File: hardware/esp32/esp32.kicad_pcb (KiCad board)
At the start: 4 copper layers, 32.8 x 36.3 mm, 69 parts, among them J1 PlugIn_Terminal_01x02, J2 ESP_left, J3 ESP_right, J4 PlugIn_Terminal_01x02, J5 Plugged into C8387, Q1 MMBT5401, Q2 MMBT2222A, U2 LMV321, U3 LMV321, U6 LM393

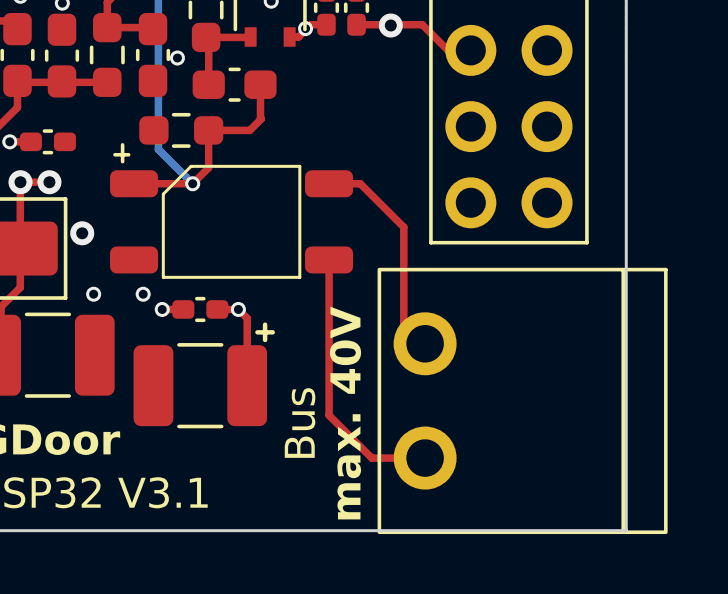
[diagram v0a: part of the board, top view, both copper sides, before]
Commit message: Release HW3.1-1
Changed bus connector due to JLCPCB availability
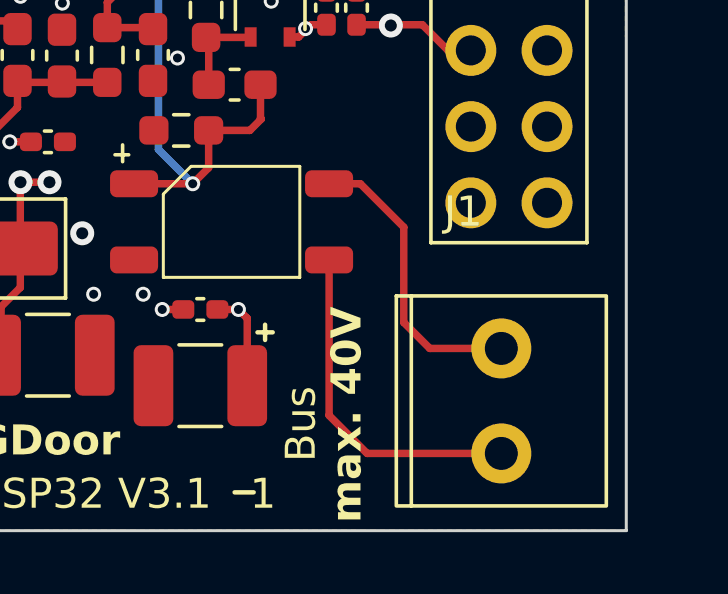
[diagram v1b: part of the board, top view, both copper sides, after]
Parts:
- removed J5: Plugged into C8387, Library:nofoorprint
- J1: value PlugIn_Terminal_01x02 -> PlugIn_Terminal_Screw; footprint Library:steckklemme2x1_1 -> Library:anschlussklemme2x1_3_5
- moved J1 2.54 mm to (140.7, 109.7)
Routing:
- net Net-(J1-Pin_1): track 7.27 -> 9.88 mm
- net Net-(J1-Pin_2): track 8.97 -> 11.4 mm
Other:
- board text added: "1"
- board text removed: "Connector C8466 (J5) plugged into C8387 (J1)"
- board text removed: "J5"
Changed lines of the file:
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@@
     )
   )
-  (footprint "Library:nofoorprint" (layer "F.Cu")
-    (at 153.543 109.3978)
-    (property "MPN" "C8466")
-    (property "Sheetfile" "esp32.kicad_sch")
-    (property "Sheetname" "")
-    (attr smd)
-    (fp_text reference "J5" (at 0 -0.5 unlocked) (layer "F.SilkS") hide
-        (effects (font (size 1 1) (thickness 0.1)))
-    )
-    (fp_text value "Plugged into C8387" (at 0 1 unlocked) (layer "F.Fab")
-        (effects (font (size 1 1) (thickness 0.15)))
-    )
-    (fp_text user "${REFERENCE}" (at 0 2.5 unlocked) (layer "F.Fab")
-        (effects (font (size 1 1) (thickness 0.15)))
-    )
-    (fp_rect (start -4.826 -5.08) (end 5.334 5.842)
-      (stroke (width 0.05) (type default)) (fill none) (layer "F.CrtYd"))
-  )
   (footprint "Library:C_0603_1608Metric_Pad1.08x0.95mm_HandSolder" (layer "F.Cu")
     (at 131.826 99.187)
@@
     )
   )
-  (footprint "Library:steckklemme2x1_1" (layer "F.Cu")
-    (at 138.176 109.728)
+  (footprint "Library:anschlussklemme2x1_3_5" (layer "F.Cu")
+    (at 140.716 109.728)
     (property "JLCPCB Rotation Offset" "90")
     (property "JlcRotOffset" "-180")
-    (property "MPN" "C8387")
+    (property "MPN" "C695629")
     (property "Sheetfile" "esp32.kicad_sch")
     (property "Sheetname" "")
@@
     (property "ki_keywords" "screw terminal")
     (attr through_hole)
-    (fp_text reference "J1" (at -1.27 -6.31 unlocked) (layer "F.SilkS") hide
+    (fp_text reference "J1" (at -1.27 -6.31 unlocked) (layer "F.SilkS")
         (effects (font (size 1 1) (thickness 0.15)))
     )
-    (fp_text value "PlugIn_Terminal_01x02" (at 0 -1.5 unlocked) (layer "F.Fab")
+    (fp_text value "PlugIn_Terminal_Screw" (at 0 -1.5 unlocked) (layer "F.Fab")
         (effects (font (size 1 1) (thickness 0.15)))
     )
@@
         (effects (font (size 1 1) (thickness 0.15)))
     )
-    (fp_line (start 6.604 -4.318) (end 6.604 4.318)
+    (fp_line (start -3 -3.5) (end -3 3.5)
       (stroke (width 0.12) (type solid)) (layer "F.SilkS"))
-    (fp_rect (start 8.024 -4.377) (end -1.524 4.377)
+    (fp_rect (start -3.5 -3.5) (end 3.5 3.5)
       (stroke (width 0.12) (type solid)) (fill none) (layer "F.SilkS"))
-    (pad "1" thru_hole circle (at 0 -1.905) (size 2.1 2.1) (drill 1.25) (layers "*.Cu" "*.Mask")
+    (pad "1" thru_hole circle (at 0 -1.75) (size 2 2) (drill 1.1) (layers "*.Cu" "*.Mask")
       (net 12 "Net-(J1-Pin_1)") (pinfunction "Pin_1") (pintype "passive"))
-    (pad "2" thru_hole circle (at 0 1.905) (size 2.1 2.1) (drill 1.25) (layers "*.Cu" "*.Mask")
+    (pad "2" thru_hole circle (at 0 1.75) (size 2 2) (drill 1.1) (layers "*.Cu" "*.Mask")
       (net 13 "Net-(J1-Pin_2)") (pinfunction "Pin_2") (pintype "passive"))
-    (model "${KIPRJMOD}/3dmodels/screwterminal.stp"
-      (offset (xyz 8 4.22 7))
+    (model "${KIPRJMOD}/3dmodels/screwterminal_3_5mm_2.STEP"
+      (offset (xyz 3.6 -3.5 0))
       (scale (xyz 1 1 1))
-      (rotate (xyz 180 0 90))
+      (rotate (xyz -90 0 -90))
     )
   )
@@
   (gr_circle (center 142.24 87.884) (end 143.129 88.265)
     (stroke (width 0.15) (type default)) (fill none) (layer "B.SilkS"))
-  (gr_rect (start 136.525 105.537) (end 141.478 113.411)
+  (gr_rect (start 138.7475 105.537) (end 143.7005 113.411)
     (stroke (width 0.15) (type default)) (fill none) (layer "B.SilkS"))
   (gr_line (start 125.781295 107.297593) (end 125.789967 107.292438)
@@
   (gr_line (start 122.428 107.315) (end 122.936 107.315)
     (stroke (width 0.15) (type default)) (layer "F.SilkS"))
+  (gr_line (start 131.826 112.776) (end 132.461 112.776)
+    (stroke (width 0.15) (type default)) (layer "F.SilkS"))
   (gr_line (start 122.682 107.061) (end 122.682 107.569)
     (stroke (width 0.15) (type default)) (layer "F.SilkS"))
@@
   (gr_line (start 120.65 111.76) (end 122.174 111.76)
     (stroke (width 0.3) (type default)) (layer "F.SilkS"))
-  (gr_line (start 148.59 108.966) (end 146.939 109.728)
-    (stroke (width 0.15) (type default)) (layer "Cmts.User"))
-  (gr_line (start 155.575 109.728) (end 146.939 109.728)
-    (stroke (width 0.15) (type default)) (layer "Cmts.User"))
-  (gr_line (start 146.939 109.728) (end 148.59 108.966)
-    (stroke (width 0.15) (type default)) (layer "Cmts.User"))
-  (gr_line (start 148.59 110.49) (end 146.939 109.728)
-    (stroke (width 0.15) (type default)) (layer "Cmts.User"))
   (gr_rect (start 112.052 77.743) (end 144.8816 114.0524)
     (stroke (width 0.1) (type default)) (fill none) (layer "Edge.Cuts"))
@@
     (effects (font (size 1 1) (thickness 0.15)) (justify left bottom mirror))
   )
-  (gr_text "A" (at 140.208 107.9754) (layer "B.SilkS")
+  (gr_text "A" (at 139.319 107.061) (layer "B.SilkS")
     (effects (font (size 1 1) (thickness 0.15)) (justify bottom mirror))
   )
@@
     (effects (font (size 1 1) (thickness 0.15)) (justify left top mirror))
   )
-  (gr_text "Bus" (at 142.0368 109.1692 270) (layer "B.SilkS")
+  (gr_text "Bus" (at 142.24 109.728 270) (layer "B.SilkS")
     (effects (font (size 1 1) (thickness 0.2) bold) (justify bottom mirror))
   )
@@
     (effects (font (size 1 1) (thickness 0.2) bold) (justify left bottom mirror))
   )
-  (gr_text "B" (at 140.1826 111.8616) (layer "B.SilkS")
+  (gr_text "B" (at 139.319 113.157) (layer "B.SilkS")
     (effects (font (size 1 1) (thickness 0.15)) (justify bottom mirror))
   )
@@
     (effects (font (size 1 1) (thickness 0.25) bold) (justify left bottom))
   )
+  (gr_text "1" (at 132.334 113.411) (layer "F.SilkS")
+    (effects (font (size 1 1) (thickness 0.15)) (justify left bottom))
+  )
   (gr_text "ESP32 V3.1" (at 123.19 113.411) (layer "F.SilkS")
     (effects (font (size 1 1) (thickness 0.15)) (justify left bottom))
@@
     (effects (font (size 1 1) (thickness 0.15)) (justify left bottom))
   )
-  (gr_text "J5" (at 152.654 112.522) (layer "Cmts.User")
-    (effects (font (size 1 1) (thickness 0.15)) (justify left bottom))
-  )
-  (gr_text "Connector C8466 (J5)\nplugged into C8387 (J1)" (at 141.478 117.729) (layer "Cmts.User")
-    (effects (font (size 1 1) (thickness 0.15)) (justify left bottom))
-  )
   (dimension (type aligned) (layer "User.1")
     (pts (xy 144.8816 77.7748) (xy 144.907 72.6186))
@@
   (segment (start 129.0563 97.2839) (end 129.1063 97.3339) (width 0.25) (layer "F.Cu") (net 11))
   (segment (start 128.0884 94.1832) (end 128.0884 95.6564) (width 0.25) (layer "F.Cu") (net 11))
-  (segment (start 136.017 102.489) (end 134.9744 102.489) (width 0.25) (layer "F.Cu") (net 12))
-  (segment (start 138.176 107.823) (end 137.4648 107.1118) (width 0.25) (layer "F.Cu") (net 12))
-  (segment (start 137.4648 107.1118) (end 137.4648 103.9368) (width 0.25) (layer "F.Cu") (net 12))
-  (segment (start 137.4648 103.9368) (end 136.017 102.489) (width 0.25) (layer "F.Cu") (net 12))
+  (segment (start 137.4648 103.9368) (end 137.4648 107.1118) (width 0.25) (layer "F.Cu") (net 12))
+  (segment (start 136.017 102.489) (end 137.4648 103.9368) (width 0.25) (layer "F.Cu") (net 12))
+  (segment (start 138.331 107.978) (end 140.716 107.978) (width 0.25) (layer "F.Cu") (net 12))
+  (segment (start 134.9744 102.489) (end 136.017 102.489) (width 0.25) (layer "F.Cu") (net 12))
+  (segment (start 137.4648 107.1118) (end 138.331 107.978) (width 0.25) (layer "F.Cu") (net 12))
   (segment (start 134.9744 105.029) (end 134.9744 110.2094) (width 0.25) (layer "F.Cu") (net 13))
-  (segment (start 136.398 111.633) (end 138.176 111.633) (width 0.25) (layer "F.Cu") (net 13))
-  (segment (start 134.9744 110.2094) (end 136.398 111.633) (width 0.25) (layer "F.Cu") (net 13))
+  (segment (start 136.243 111.478) (end 140.716 111.478) (width 0.25) (layer "F.Cu") (net 13))
+  (segment (start 134.9744 110.2094) (end 136.243 111.478) (width 0.25) (layer "F.Cu") (net 13))
   (segment (start 130.3141 83.2872) (end 130.9226 82.6787) (width 0.25) (layer "F.Cu") (net 14))
   (segment (start 130.9226 82.6787) (end 130.9226 82.2173) (width 0.25) (layer "F.Cu") (net 14))

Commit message: work on V4.0
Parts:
- added C21: 100u TBD check voltage, Library:C_1210_3225Metric_Pad1.33x2.70mm_HandSolder, F.Cu at (109.2, 97.4)
- added C22: 100n, Library:C_0603_1608Metric_Pad1.08x0.95mm_HandSolder, F.Cu at (100.6, 87.8)
- added C23: 10u, Library:C_0603_1608Metric_Pad1.08x0.95mm_HandSolder, F.Cu at (105.5, 87.8)
- added C24: 100n, Library:C_0603_1608Metric_Pad1.08x0.95mm_HandSolder, F.Cu at (104.0, 87.8)
- added C25: 10u, Library:C_0603_1608Metric_Pad1.08x0.95mm_HandSolder, F.Cu at (108.7, 93.2)
- added C26: 100n, Library:C_0603_1608Metric_Pad1.08x0.95mm_HandSolder, F.Cu at (107.2, 93.2)
- added C27: 10u, Library:C_0603_1608Metric_Pad1.08x0.95mm_HandSolder, F.Cu at (105.5, 93.2)
- added C28: 10u, Library:C_0603_1608Metric_Pad1.08x0.95mm_HandSolder, F.Cu at (107.1, 80.9)
- added C29: 10u, Library:C_0603_1608Metric_Pad1.08x0.95mm_HandSolder, F.Cu at (107.1, 79.4)
- added C30: 10u, Library:C_0603_1608Metric_Pad1.08x0.95mm_HandSolder, F.Cu at (107.1, 84.7)
- added C31: 10u, Library:C_0603_1608Metric_Pad1.08x0.95mm_HandSolder, F.Cu at (107.1, 83.2)
- added C32: 100n, Library:C_0603_1608Metric_Pad1.08x0.95mm_HandSolder, F.Cu at (102.2, 102.5)
- added C33: 100n, Library:C_0603_1608Metric_Pad1.08x0.95mm_HandSolder, F.Cu at (107.3, 108.7)
- added C34: 100n, Library:C_0603_1608Metric_Pad1.08x0.95mm_HandSolder, F.Cu at (104.0, 93.2)
- added C35: 10u, Library:C_0603_1608Metric_Pad1.08x0.95mm_HandSolder, F.Cu at (102.1, 87.8)
- added C36: 100n, Library:C_0402_1005Metric_Pad0.74x0.62mm_HandSolder, F.Cu at (99.9, 95.5)
- added C37: 10u, Library:C_0603_1608Metric_Pad1.08x0.95mm_HandSolder, F.Cu at (92.5, 102.6)
- added C38: 100n, Library:C_0402_1005Metric_Pad0.74x0.62mm_HandSolder, F.Cu at (94.6, 92.5)
- added C39: 10u, Library:C_0603_1608Metric_Pad1.08x0.95mm_HandSolder, F.Cu at (86.4, 102.6)
- added C40: 100n, Library:C_0402_1005Metric_Pad0.74x0.62mm_HandSolder, F.Cu at (94.6, 94.1)
- added C41: 10u, Library:C_0603_1608Metric_Pad1.08x0.95mm_HandSolder, F.Cu at (89.4, 102.6)
- added C42: 100n, Library:C_0402_1005Metric_Pad0.74x0.62mm_HandSolder, F.Cu at (102.0, 93.2)
- added C43: 10u, Library:C_0603_1608Metric_Pad1.08x0.95mm_HandSolder, F.Cu at (95.5, 102.6)
- added C44: 22p, Library:C_0603_1608Metric_Pad1.08x0.95mm_HandSolder, F.Cu at (89.7, 91.9)
- added C45: 22p, Library:C_0603_1608Metric_Pad1.08x0.95mm_HandSolder, F.Cu at (93.6, 88.5)
- added C46: 100n, Library:C_0402_1005Metric_Pad0.74x0.62mm_HandSolder, F.Cu at (86.6, 107.0)
- added C47: 10u, Library:C_0603_1608Metric_Pad1.08x0.95mm_HandSolder, F.Cu at (87.9, 107.2)
- added C48: 22p, Library:C_0603_1608Metric_Pad1.08x0.95mm_HandSolder, F.Cu at (92.6, 95.4)
- added C49: 22p, Library:C_0603_1608Metric_Pad1.08x0.95mm_HandSolder, F.Cu at (96.6, 98.0)
- added C50: 22p, Library:C_0603_1608Metric_Pad1.08x0.95mm_HandSolder, F.Cu at (92.7, 91.9)
- added C51: 100n, Library:C_0402_1005Metric_Pad0.74x0.62mm_HandSolder, F.Cu at (89.7, 107.0)
- added C52: 10u, Library:C_0603_1608Metric_Pad1.08x0.95mm_HandSolder, F.Cu at (90.9, 107.2)
- added C53: 100n, Library:C_0402_1005Metric_Pad0.74x0.62mm_HandSolder, F.Cu at (92.7, 107.0)
- added C54: 10u, Library:C_0603_1608Metric_Pad1.08x0.95mm_HandSolder, F.Cu at (94.0, 107.2)
- added C55: 100n, Library:C_0402_1005Metric_Pad0.74x0.62mm_HandSolder, F.Cu at (95.8, 107.0)
- added C56: 10u, Library:C_0603_1608Metric_Pad1.08x0.95mm_HandSolder, F.Cu at (97.0, 107.2)
- added C57: 100u, Library:C_1210_3225Metric_Pad1.33x2.70mm_HandSolder, F.Cu at (107.0, 111.1)
- added C59: 100u, Library:C_1210_3225Metric_Pad1.33x2.70mm_HandSolder, F.Cu at (99.8, 107.4)
- added C61: 22p, Library:C_0603_1608Metric_Pad1.08x0.95mm_HandSolder, F.Cu at (103.5, 105.8)
- added C62: 100n, Library:C_0402_1005Metric_Pad0.74x0.62mm_HandSolder, F.Cu at (102.4, 84.7)
- added C63: 100n, Library:C_0402_1005Metric_Pad0.74x0.62mm_HandSolder, F.Cu at (102.4, 80.6)
- added R35: 82k, Library:R_0603_1608Metric_Pad0.98x0.95mm_HandSolder, F.Cu at (110.6, 88.0)
- added R37: 1k, Library:R_0603_1608Metric_Pad0.98x0.95mm_HandSolder, F.Cu at (91.8, 84.4)
- added R38: 1k, Library:R_0603_1608Metric_Pad0.98x0.95mm_HandSolder, F.Cu at (88.8, 84.4)
- added R39: 1k, Library:R_0603_1608Metric_Pad0.98x0.95mm_HandSolder, F.Cu at (97.9, 84.4)
- added R40: 1k, Library:R_0603_1608Metric_Pad0.98x0.95mm_HandSolder, F.Cu at (94.9, 84.4)
- added R41: 33, Library:R_0603_1608Metric_Pad0.98x0.95mm_HandSolder, F.Cu at (97.0, 102.6)
- added R42: 33, Library:R_0603_1608Metric_Pad0.98x0.95mm_HandSolder, F.Cu at (90.9, 102.6)
- added R43: 33, Library:R_0603_1608Metric_Pad0.98x0.95mm_HandSolder, F.Cu at (87.9, 102.6)
- added R44: 33, Library:R_0603_1608Metric_Pad0.98x0.95mm_HandSolder, F.Cu at (94.0, 102.6)
- added R45: 10k, Library:R_0402_1005Metric_Pad0.72x0.64mm_HandSolder, F.Cu at (94.9, 88.9)
- added R46: 2k4, Library:R_0603_1608Metric_Pad0.98x0.95mm_HandSolder, F.Cu at (90.6, 88.5)
- added R47: 2k4, Library:R_0603_1608Metric_Pad0.98x0.95mm_HandSolder, F.Cu at (88.1, 95.4)
- added R48: 100, Library:R_0603_1608Metric_Pad0.98x0.95mm_HandSolder, F.Cu at (88.1, 91.9)
- added R49: 100, Library:R_0603_1608Metric_Pad0.98x0.95mm_HandSolder, F.Cu at (92.1, 88.5)
- added R50: 33, Library:R_0603_1608Metric_Pad0.98x0.95mm_HandSolder, F.Cu at (91.2, 91.9)
- added R51: 33, Library:R_0603_1608Metric_Pad0.98x0.95mm_HandSolder, F.Cu at (95.1, 98.0)
- added R52: 33, Library:R_0603_1608Metric_Pad0.98x0.95mm_HandSolder, F.Cu at (92.6, 96.9)
- added R53: 33, Library:R_0603_1608Metric_Pad0.98x0.95mm_HandSolder, F.Cu at (92.6, 99.4)
- added R54: 33, Library:R_0603_1608Metric_Pad0.98x0.95mm_HandSolder, F.Cu at (98.2, 98.0)
- added R55: 0, Library:R_0603_1608Metric_Pad0.98x0.95mm_HandSolder, F.Cu at (99.7, 101.6)
- added R56: 0, Library:R_0603_1608Metric_Pad0.98x0.95mm_HandSolder, F.Cu at (120.7, 80.0)
- added R57: 0, Library:R_0603_1608Metric_Pad0.98x0.95mm_HandSolder, F.Cu at (110.5, 111.1)
- added R58: 0, Library:R_0603_1608Metric_Pad0.98x0.95mm_HandSolder, F.Cu at (99.7, 103.4)
- added R59: 0, Library:R_0603_1608Metric_Pad0.98x0.95mm_HandSolder, F.Cu at (97.9, 80.6)
- added R60: 0, Library:R_0603_1608Metric_Pad0.98x0.95mm_HandSolder, F.Cu at (91.8, 80.6)
- added R61: 0, Library:R_0603_1608Metric_Pad0.98x0.95mm_HandSolder, F.Cu at (94.9, 80.6)
- added R62: 0, Library:R_0603_1608Metric_Pad0.98x0.95mm_HandSolder, F.Cu at (88.8, 80.6)
- added R63: 0, Library:R_0603_1608Metric_Pad0.98x0.95mm_HandSolder, F.Cu at (93.3, 80.6)
- added R64: 0, Library:R_0603_1608Metric_Pad0.98x0.95mm_HandSolder, F.Cu at (99.4, 80.6)
- added R65: 0, Library:R_0603_1608Metric_Pad0.98x0.95mm_HandSolder, F.Cu at (96.4, 80.6)
- added R66: 0, Library:R_0603_1608Metric_Pad0.98x0.95mm_HandSolder, F.Cu at (90.3, 80.6)
- added R67: 0, Library:R_0603_1608Metric_Pad0.98x0.95mm_HandSolder, F.Cu at (102.0, 96.6)
- added R68: 0, Library:R_0603_1608Metric_Pad0.98x0.95mm_HandSolder, F.Cu at (99.7, 98.0)
- added R69: 1k, Library:R_0603_1608Metric_Pad0.98x0.95mm_HandSolder, F.Cu at (96.4, 84.4)
- added R70: 1k, Library:R_0603_1608Metric_Pad0.98x0.95mm_HandSolder, F.Cu at (99.4, 84.4)
- added R71: 1k, Library:R_0603_1608Metric_Pad0.98x0.95mm_HandSolder, F.Cu at (90.3, 84.4)
- added R72: 1k, Library:R_0603_1608Metric_Pad0.98x0.95mm_HandSolder, F.Cu at (93.3, 84.4)
- added R73: 10k, Library:R_0603_1608Metric_Pad0.98x0.95mm_HandSolder, F.Cu at (109.1, 88.0)
- added U5: ES8374, Library:QFN-28-1EP_4x4mm_P0.4mm_EP2.3x2.3mm, F.Cu at (98.4, 92.1)
- added U7: AMS1117-3.3, Library:SOT-223-3_TabPin2, F.Cu at (108.0, 103.5)
- R27: value 4k7 -> 18k
- R32: value 100k -> 22
- moved R32 24.4 mm to (105.9, 97.4), turned to -90 degrees
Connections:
- J2 pad 14: unconnected-(J2-IO_05/D8-Pad14) -> /I2S_SCLK
- J2 pad 6: /RX_THRESH -> /I2S_DSDIN
- J2 pad 7: unconnected-(J2-IO_35-Pad7) -> /I2S_ASDOUT
- J3 pad 10: unconnected-(J3-IO_12/TDI-Pad10) -> /TX
- J3 pad 14: unconnected-(J3-IO_00-Pad14) -> /I2S_MCLK
- J3 pad 6: /TX -> /I2S_LRCK
- R22 pad 2: /RX_THRESH -> GND
- R27 pad 2: /RX_ANA -> GND
- R30 pad 1: /RX_DAC -> Net-(R30-Pad1)
- R31 pad 1: /RX_DAC -> Net-(R30-Pad1)
- R32 pad 1: Net-(D1-+) -> Net-(U5A-MONOOUT)
- R32 pad 2: GND -> Net-(C21-Pad1)
- U6 pad 7: /RX_DAC -> Net-(R30-Pad1)
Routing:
- net /I2S_LRCK: track 0.00 -> 72.1 mm, vias 0 -> 1
- net /I2S_MCLK: track 0.00 -> 61.5 mm, vias 0 -> 1
- net Net-(D1-+): track 17.7 -> 64.1 mm, vias 2 -> 4
- net /I2S_DSDIN: track 0.00 -> 32.7 mm, vias 0 -> 2
- net /I2S_ASDOUT: track 0.00 -> 30.3 mm, vias 0 -> 1
- net /I2S_SCLK: track 0.00 -> 29.3 mm, vias 0 -> 1
- net Net-(C46-Pad2): track 0.00 -> 29.3 mm
- net +3.3V_ANA: track 0.00 -> 22.0 mm
- net Net-(C29-Pad1): track 0.00 -> 17.6 mm, vias 0 -> 2
- net Net-(U5D-PVDD): track 0.00 -> 16.6 mm, vias 0 -> 2
- net +5V: track 15.5 -> 31.3 mm, vias 6 -> 8
- net Net-(U5D-AVDD): track 0.00 -> 15.1 mm, vias 0 -> 2
- net Net-(U5D-SPKVDD): track 0.00 -> 14.7 mm, vias 0 -> 2
- net Net-(C28-Pad1): track 0.00 -> 14.1 mm, vias 0 -> 2
- net Net-(U5D-DVDD): track 0.00 -> 13.9 mm, vias 0 -> 2
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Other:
- board size 32.8 x 36.3 mm -> 60.8 x 36.3 mm
- board text added: "ESP32 V4.0"
- board text added: "I2S_DIN"
- board text added: "I2S_LRCK"
- board text added: "I2S_MCLK"
- board text removed: "1"
- board text removed: "ESP32 V3.1"
- board text removed: "RX_THRESH"

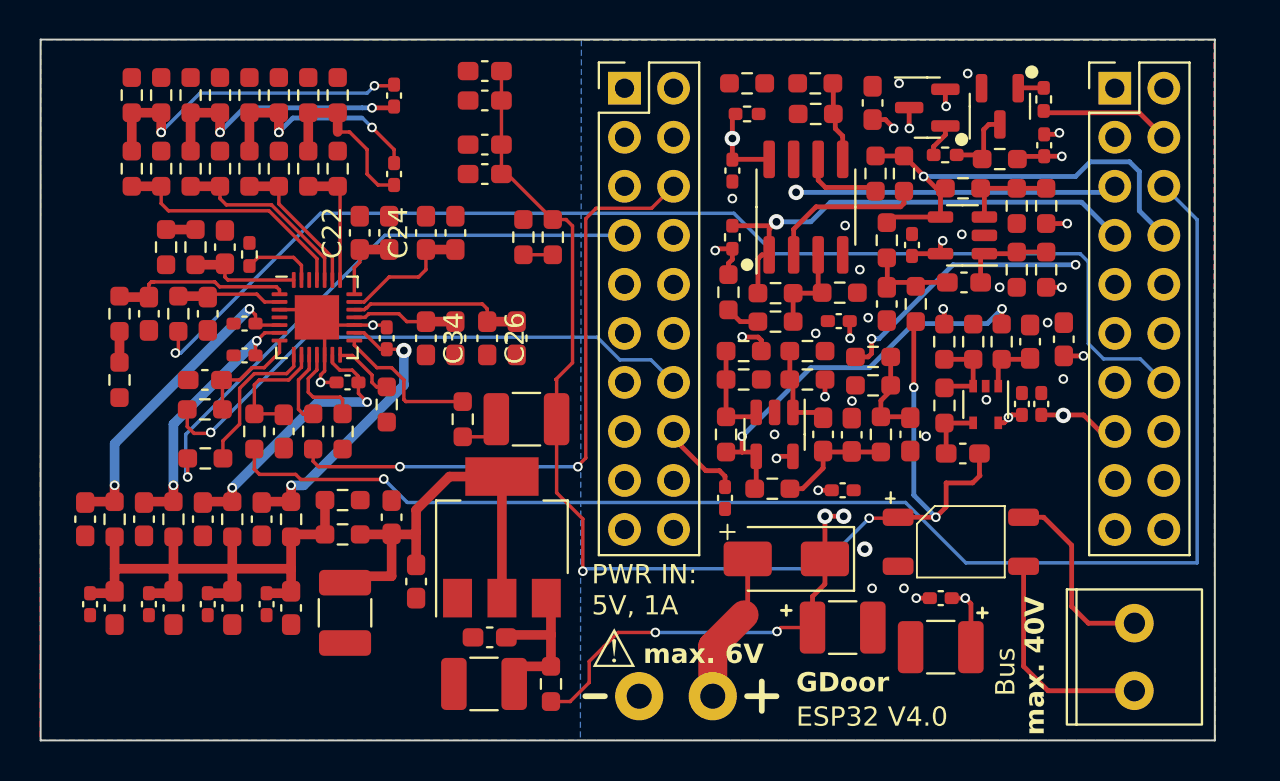
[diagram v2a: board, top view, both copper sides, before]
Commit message: First layout with DRC check on V4.0
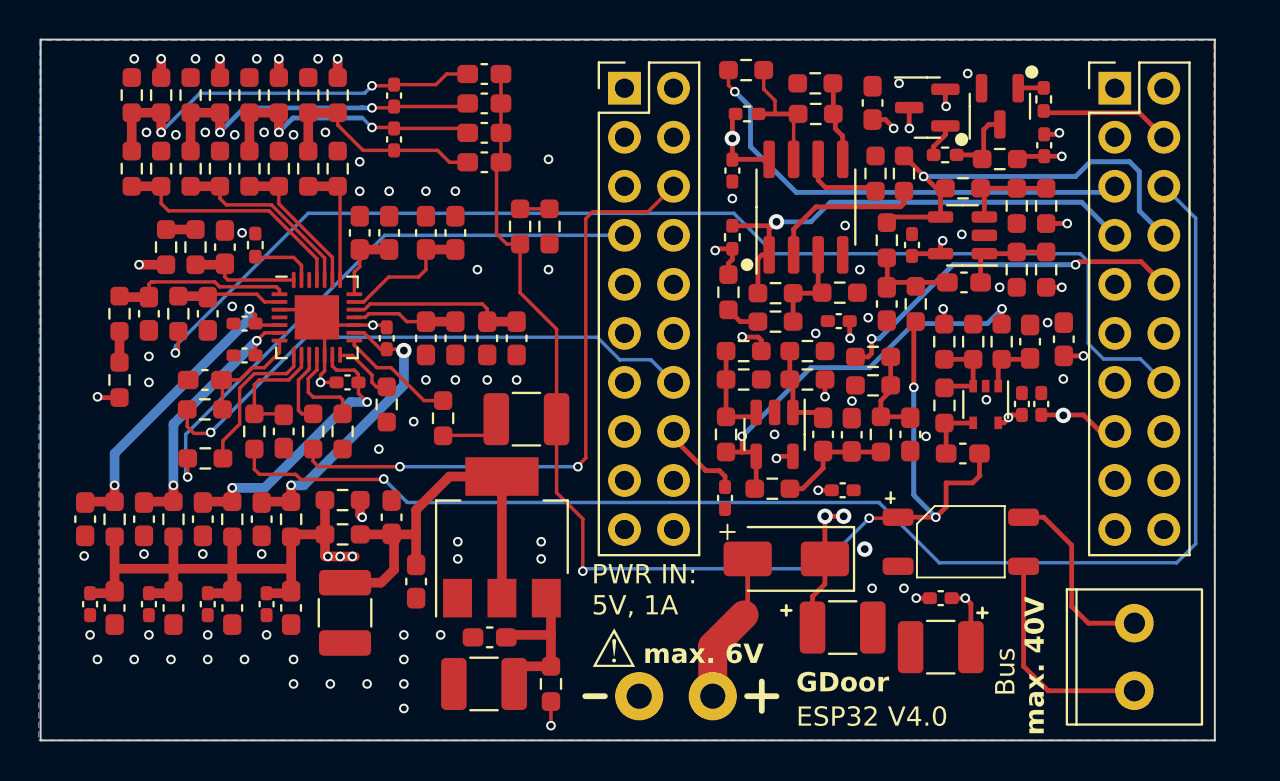
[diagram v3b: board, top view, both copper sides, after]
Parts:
- moved C62 1.79 mm to (102.4, 82.9)
- moved R35 1.78 mm to (108.9, 87.4), turned to -90 degrees
- moved R73 1.46 mm to (110.4, 87.4), turned to -90 degrees
- moved R32 1.02 mm to (104.9, 97.4)
- moved R56 0.69 mm to (120.6, 79.3)
- moved C30 0.61 mm to (107.0, 84.1)
- moved C31 0.61 mm to (107.0, 82.6)
- moved R45 0.57 mm to (95.2, 88.4)
- moved C28 0.15 mm to (107.0, 81.1)
- moved C29 0.15 mm to (107.0, 79.5)
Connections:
- C46 pad 2: Net-(C46-Pad2) -> +3.3V_AUDIO
- C47 pad 2: Net-(C46-Pad2) -> +3.3V_AUDIO
- C51 pad 2: Net-(C46-Pad2) -> +3.3V_AUDIO
- C52 pad 2: Net-(C46-Pad2) -> +3.3V_AUDIO
- C53 pad 2: Net-(C46-Pad2) -> +3.3V_AUDIO
- C54 pad 2: Net-(C46-Pad2) -> +3.3V_AUDIO
- C55 pad 2: Net-(C46-Pad2) -> +3.3V_AUDIO
- C56 pad 2: Net-(C46-Pad2) -> +3.3V_AUDIO
- R41 pad 2: Net-(C46-Pad2) -> +3.3V_AUDIO
- R42 pad 2: Net-(C46-Pad2) -> +3.3V_AUDIO
- R43 pad 2: Net-(C46-Pad2) -> +3.3V_AUDIO
- R44 pad 2: Net-(C46-Pad2) -> +3.3V_AUDIO
- R46 pad 1: +3.3V -> +3.3V_AUDIO
- R47 pad 1: +3.3V -> +3.3V_AUDIO
- R55 pad 1: Net-(C46-Pad2) -> +3.3V_AUDIO
- R58 pad 1: Net-(C46-Pad2) -> +3.3V_AUDIO
- R63 pad 1: +3.3V_ANA -> +3.3V_AUDIO
- R64 pad 1: +3.3V_ANA -> +3.3V_AUDIO
- R65 pad 1: +3.3V_ANA -> +3.3V_AUDIO
- R66 pad 1: +3.3V_ANA -> +3.3V_AUDIO
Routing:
- net +3.3V_AUDIO: track 0.00 -> 38.4 mm, vias 0 -> 9
- net Net-(C46-Pad2): track 29.3 -> 0.00 mm
- net +5Vonoff: track 8.49 -> 27.0 mm
- net +5V: track 31.3 -> 16.7 mm, vias 8 -> 7
- net /RX_DAC: track 16.8 -> 24.4 mm
- net Net-(R30-Pad1): track 0.33 -> 7.04 mm
- net /TX: track 13.8 -> 19.0 mm
- net Net-(C29-Pad1): track 17.6 -> 21.7 mm
- net Net-(C28-Pad1): track 14.1 -> 18.0 mm
- net +3.3V: track 20.0 -> 22.8 mm, vias 7 -> 8
- net Net-(C31-Pad1): track 12.2 -> 14.9 mm
- net Net-(C30-Pad1): track 9.31 -> 11.7 mm
- net Net-(U5A-MONOOUT): track 7.66 -> 6.03 mm
- net /RX_ANA: track 24.4 -> 22.9 mm
- net Net-(C21-Pad1): track 2.65 -> 3.34 mm
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- added copper zone on In2.Cu, net +3.3V
- added copper zone on In2.Cu, net +3.3V_AUDIO
- added copper zone on In1.Cu, net GND
- removed copper zone on In1.Cu, net +3.3V
